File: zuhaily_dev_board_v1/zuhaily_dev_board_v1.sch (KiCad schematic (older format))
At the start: 42 parts

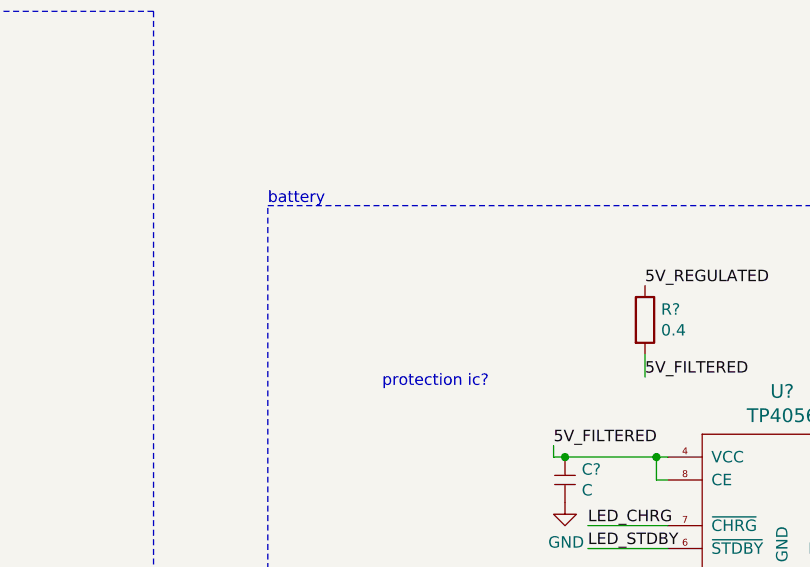
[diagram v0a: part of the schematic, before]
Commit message: added battery protection ic and testing git
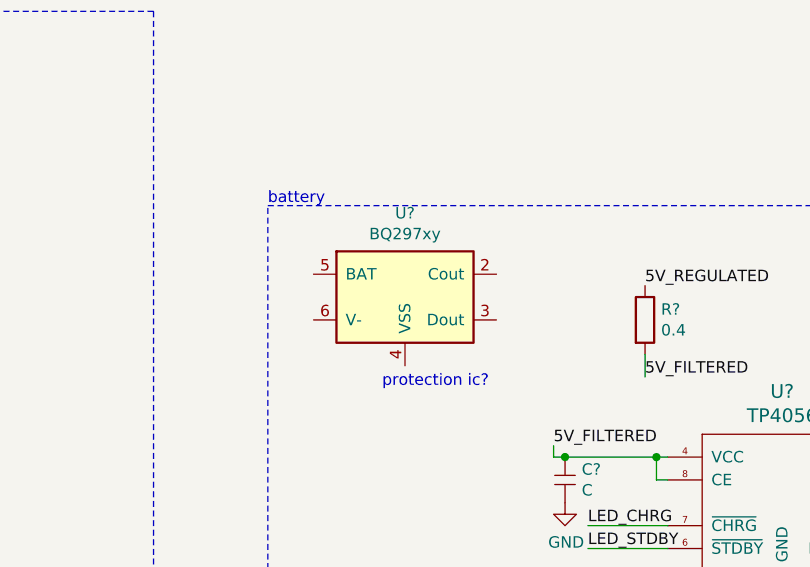
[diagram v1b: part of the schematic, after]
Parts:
- added U?: BQ297xy, Package_SON:WSON-6_1.5x1.5mm_P0.5mm, symbol Battery_Management:BQ297xy
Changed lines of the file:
@@
 Text Notes 17300 3150 0    50   ~ 0
 how to choose between usb vs batt?\n
+$Comp
+L Battery_Management:BQ297xy U?
+U 1 1 5C50F073
+P 15150 2550
+F 0 "U?" H 15150 2917 50  0000 C CNN
+F 1 "BQ297xy" H 15150 2826 50  0000 C CNN
+F 2 "Package_SON:WSON-6_1.5x1.5mm_P0.5mm" H 15150 2900 50  0001 C CNN
+F 3 "http://www.ti.com/lit/ds/symlink/bq2970.pdf" H 14900 2750 50  0001 C CNN
+	1    15150 2550
+	1    0    0    -1
+$EndComp
 $EndSCHEMATC

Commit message: added dc/usb switcher
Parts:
- added D?: DIODE, symbol pspice:DIODE
- added J?: DC_JACK, symbol tinkerforge:DC_JACK
- added Q?: MOSFET_P_CH, symbol tinkerforge:MOSFET_P_CH
- added R? (x2): 10K, symbol Device:R
- added U?: LMV358, symbol Amplifier_Operational:LMV358
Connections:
- net 3.3V_REGULATED: now also U?.2 (-)
- net 5V_REGULATED: now also Q?.D
- net GND: now also J?.1, J?.3, R?.2
- net USB_VCC: now also Q?.S; no longer U?.3 (VI)
- new net: D?.1 (K), J?.2
- new net: R?.1, R?.2, U?.3 (+)
- new net: Q?.G, U?.1
- new net 5V_REGULATOR_IN: D?.2 (A), R?.1, U?.3 (VI)
- no-connect marks 0 -> 1
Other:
- note added: "DC/usb switcher\n"
- note added: "also not sure why vin is divided by 2\n"
- note added: "not sure why it's compared to 3.3v\n"
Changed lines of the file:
@@
 EELAYER 26 0
 EELAYER END
-$Descr User 19685 11811
+$Descr User 39370 11811
 encoding utf-8
 Sheet 1 1
@@
 Wire Wire Line
 	4000 5700 3550 5700
-Text Label 3200 1650 0    50   ~ 0
-USB_VCC
-Wire Wire Line
-	3200 1650 3200 1850
+Text Label 3200 1550 0    50   ~ 0
+5V_REGULATOR_IN
+Wire Wire Line
+	3200 1550 3200 1850
 Text Label 4950 6100 0    50   ~ 0
 CH340_DTR
@@
 	1    0    0    -1
 $EndComp
+$Comp
+L tinkerforge:DC_JACK J?
+U 1 1 5C521394
+P 15250 6700
+F 0 "J?" H 15331 7037 60  0000 C CNN
+F 1 "DC_JACK" H 15331 6931 60  0000 C CNN
+F 2 "" H 15250 6700 60  0000 C CNN
+F 3 "" H 15250 6700 60  0000 C CNN
+	1    15250 6700
+	0    -1   -1   0
+$EndComp
+$Comp
+L power:GND #PWR?
+U 1 1 5C528256
+P 15200 6300
+F 0 "#PWR?" H 15200 6050 50  0001 C CNN
+F 1 "GND" H 15205 6127 50  0000 C CNN
+F 2 "" H 15200 6300 50  0001 C CNN
+F 3 "" H 15200 6300 50  0001 C CNN
+	1    15200 6300
+	0    -1   -1   0
+$EndComp
+Wire Wire Line
+	15200 6300 15200 6400
+Wire Wire Line
+	15200 6400 15450 6400
+Wire Wire Line
+	15450 6400 15450 6600
+Connection ~ 15200 6400
+NoConn ~ 17300 3550
+$Comp
+L pspice:DIODE D?
+U 1 1 5C5476D5
+P 15800 6750
+F 0 "D?" H 15800 7015 50  0000 C CNN
+F 1 "DIODE" H 15800 6924 50  0000 C CNN
+F 2 "" H 15800 6750 50  0001 C CNN
+F 3 "~" H 15800 6750 50  0001 C CNN
+	1    15800 6750
+	1    0    0    -1
+$EndComp
+Wire Wire Line
+	15600 6750 15450 6750
+$Comp
+L Device:R R?
+U 1 1 5C54DF04
+P 16650 6250
+F 0 "R?" H 16720 6296 50  0000 L CNN
+F 1 "10K" H 16720 6205 50  0000 L CNN
+F 2 "" V 16580 6250 50  0001 C CNN
+F 3 "~" H 16650 6250 50  0001 C CNN
+	1    16650 6250
+	1    0    0    -1
+$EndComp
+$Comp
+L Device:R R?
+U 1 1 5C54DF86
+P 16650 6700
+F 0 "R?" H 16720 6746 50  0000 L CNN
+F 1 "10K" H 16720 6655 50  0000 L CNN
+F 2 "" V 16580 6700 50  0001 C CNN
+F 3 "~" H 16650 6700 50  0001 C CNN
+	1    16650 6700
+	1    0    0    -1
+$EndComp
+Wire Wire Line
+	16650 6550 16650 6400
+Wire Wire Line
+	16000 6750 16000 6000
+Wire Wire Line
+	16000 6000 16650 6000
+Wire Wire Line
+	16650 6000 16650 6100
+$Comp
+L Amplifier_Operational:LMV358 U?
+U 1 1 5C5593EF
+P 17650 6650
+F 0 "U?" H 17650 7017 50  0000 C CNN
+F 1 "LMV358" H 17650 6926 50  0000 C CNN
+F 2 "" H 17650 6650 50  0001 C CNN
+F 3 "http://www.ti.com/lit/ds/symlink/lmv324.pdf" H 17650 6650 50  0001 C CNN
+	1    17650 6650
+	1    0    0    -1
+$EndComp
+Wire Wire Line
+	17350 6550 16650 6550
+Connection ~ 16650 6550
+$Comp
+L power:GND #PWR?
+U 1 1 5C55F888
+P 16650 6900
+F 0 "#PWR?" H 16650 6650 50  0001 C CNN
+F 1 "GND" H 16655 6727 50  0000 C CNN
+F 2 "" H 16650 6900 50  0001 C CNN
+F 3 "" H 16650 6900 50  0001 C CNN
+	1    16650 6900
+	1    0    0    -1
+$EndComp
+Wire Wire Line
+	16650 6900 16650 6850
+$Comp
+L tinkerforge:MOSFET_P_CH Q?
+U 1 1 5C56CE68
+P 18100 7500
+F 0 "Q?" V 18336 7500 50  0000 C CNN
+F 1 "MOSFET_P_CH" V 18427 7500 50  0000 C CNN
+F 2 "" H 18300 7600 50  0000 C CNN
+F 3 "" H 18100 7500 50  0000 C CNN
+	1    18100 7500
+	0    1    1    0
+$EndComp
+Text Label 17400 7600 0    50   ~ 0
+USB_VCC
+Wire Wire Line
+	17900 7600 17400 7600
+Wire Wire Line
+	17950 6650 18100 6650
+Wire Wire Line
+	18100 6650 18100 7300
+Text Label 16100 7500 0    50   ~ 0
+5V_REGULATOR_IN
+Wire Wire Line
+	16000 6750 16000 7500
+Wire Wire Line
+	16000 7500 16100 7500
+Connection ~ 16000 6750
+Text Label 18700 7500 0    50   ~ 0
+5V_REGULATED
+Wire Wire Line
+	18700 7500 18700 7600
+Wire Wire Line
+	18700 7600 18300 7600
+Wire Notes Line
+	19450 5850 19450 8050
+Wire Notes Line
+	19450 8050 14750 8050
+Wire Notes Line
+	14750 8050 14750 5850
+Wire Notes Line
+	14750 5850 19450 5850
+Text Notes 14800 5850 0    50   ~ 0
+DC/usb switcher\n
+Text Label 17150 7100 0    50   ~ 0
+3.3V_REGULATED
+Wire Wire Line
+	17150 7100 17150 6750
+Wire Wire Line
+	17150 6750 17350 6750
+Text Notes 16600 7250 0    50   ~ 0
+not  sure why it's compared to 3.3v\n
+Text Notes 16750 6100 0    50   ~ 0
+also not sure why vin is divided by 2\n
 $EndSCHEMATC

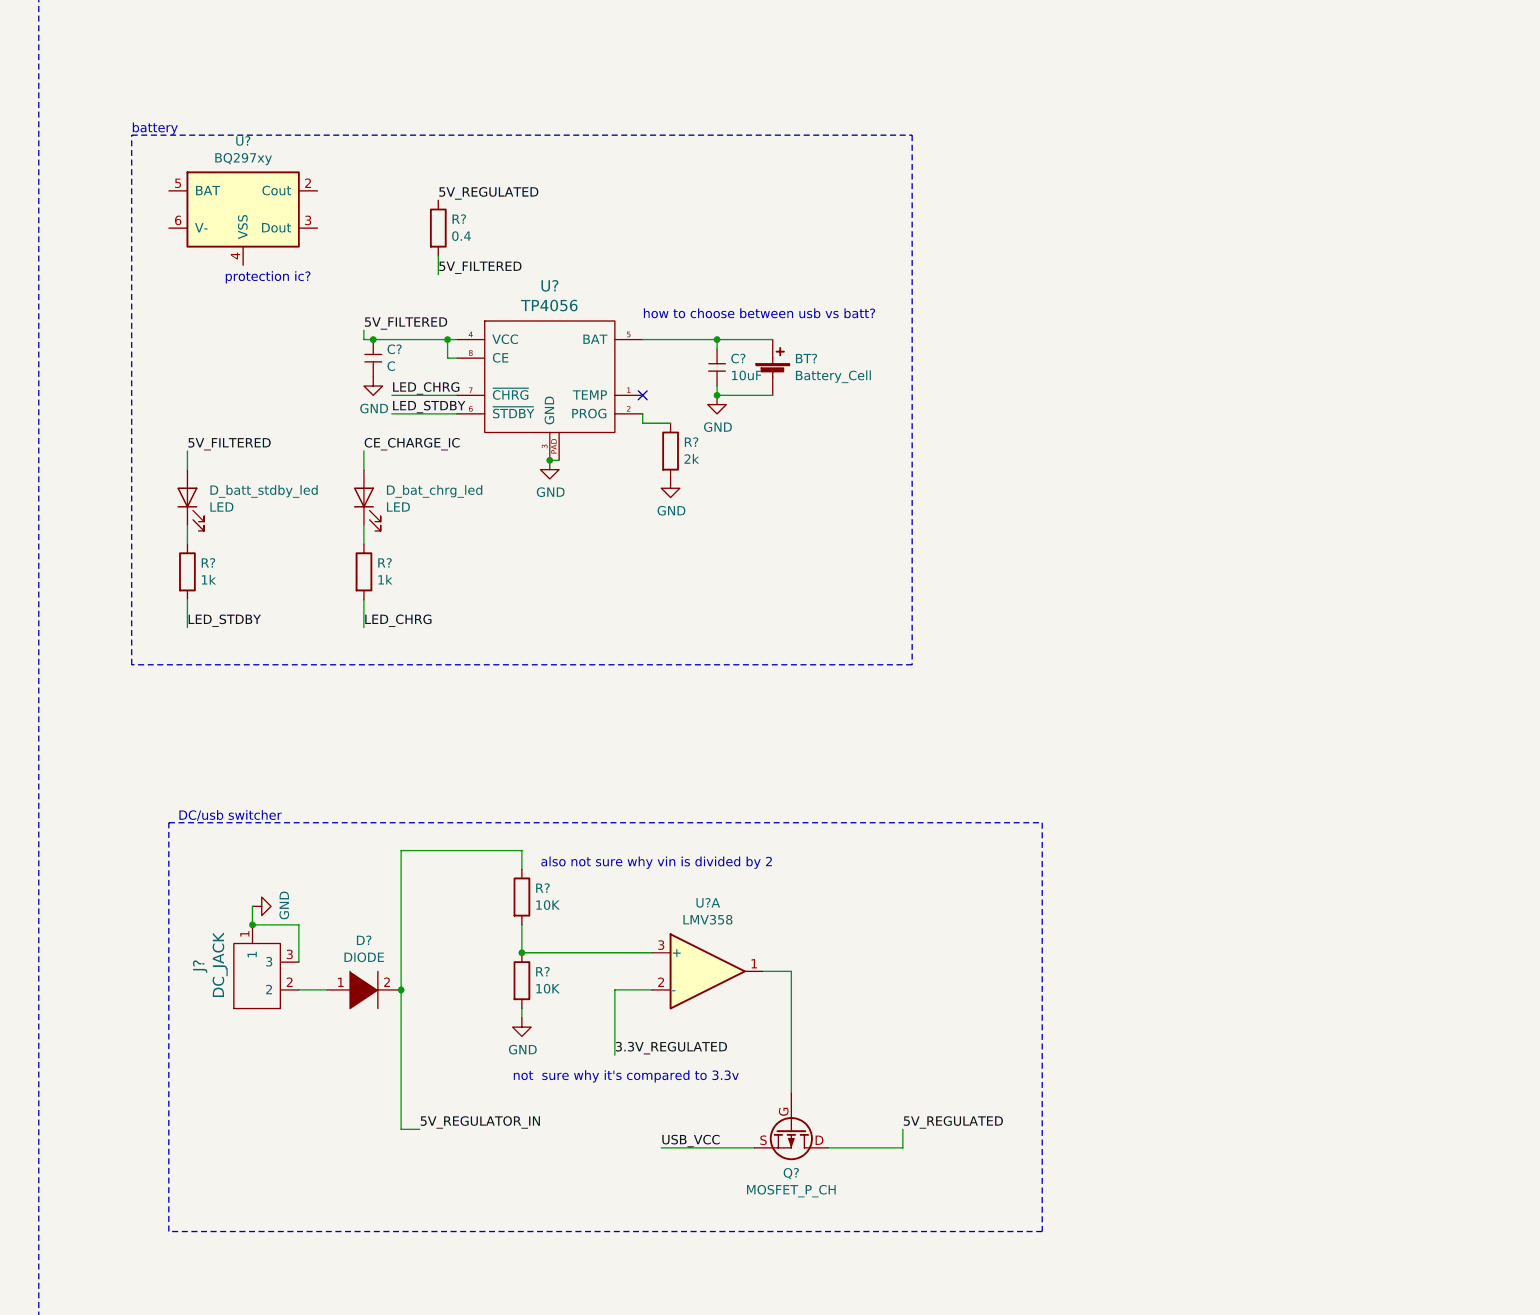
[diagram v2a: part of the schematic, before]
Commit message: added part of battery protection ic and some initial wiring
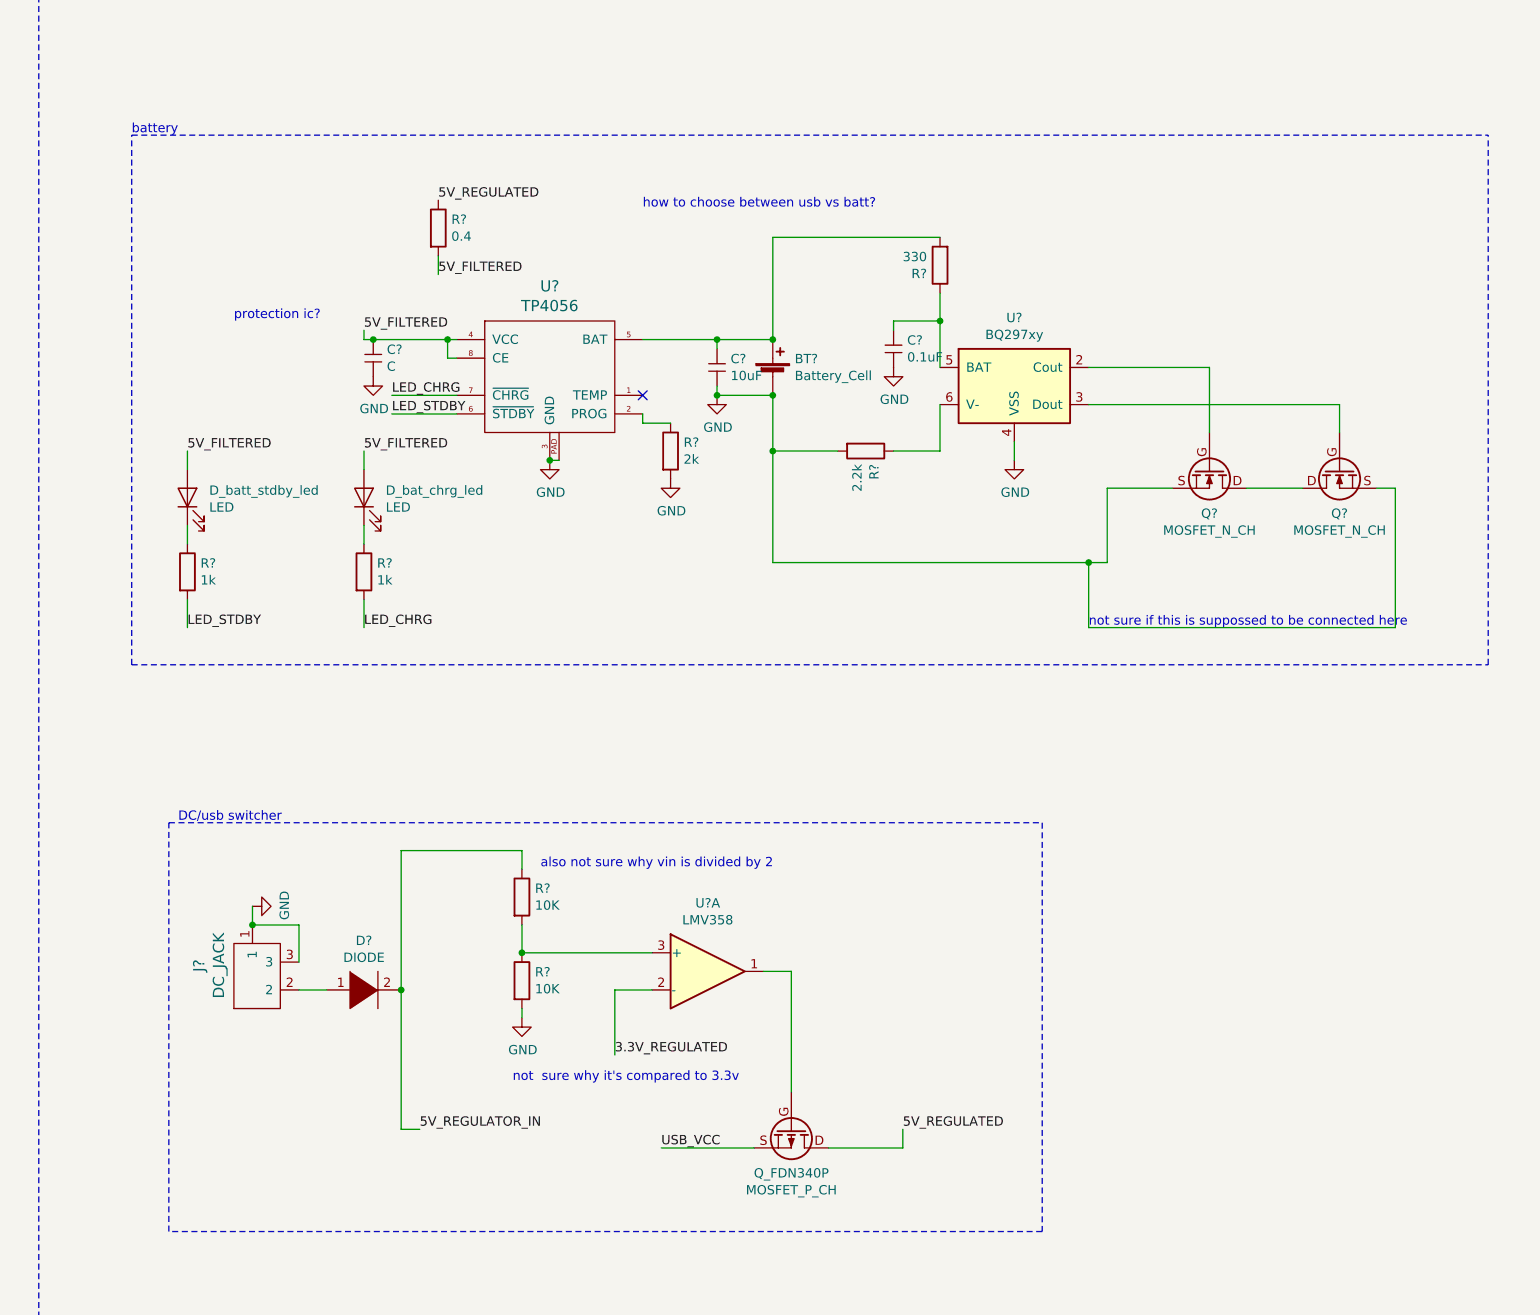
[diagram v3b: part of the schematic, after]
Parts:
- added C?: 0.1uF, symbol c:C
- added Q? (x2): MOSFET_N_CH, symbol tinkerforge:MOSFET_N_CH
- added R?: 2.2k, symbol Device:R
- added R?: 330, symbol Device:R
- gave numbers to parts that had none: 1
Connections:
- net CE_CHARGE_IC is gone; now on net 5V_FILTERED: D_bat_chrg_led.2 (A)
- net GND: now also U?.4 (VSS), C?.2, Q?.S, Q?.S, R?.2
- net at BT?.1 (+), C?.1, U?.5 (BAT): now also R?.2
- net at U?.2 (Cout): now also Q?.G
- net at U?.3 (Dout): now also Q?.G
- net at U?.5 (BAT): now also C?.1, R?.1
- net at U?.6 (V-): now also R?.1
- new net: Q?.D, Q?.D
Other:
- note added: "not sure if this is suppossed to be connected here\n"
- moved on the sheet: U?
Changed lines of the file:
@@
 $EndComp
-Wire Wire Line
-	15800 3200 15800 3250
 Wire Wire Line
 	15800 3250 15850 3250
@@
 	0    -1   -1   0
 $EndComp
-Text Label 15800 3850 0    50   ~ 0
-CE_CHARGE_IC
 Wire Wire Line
 	15800 3950 15800 3850
@@
 $EndComp
 Connection ~ 17700 3550
-Wire Notes Line
-	14550 2150 18750 2150
-Wire Notes Line
-	18750 2150 18750 5000
-Wire Notes Line
-	18750 5000 14550 5000
 Wire Notes Line
 	14550 5000 14550 2150
@@
 Text Notes 9700 9200 0    50   ~ 0
 esp 8266
-Text Notes 15050 2950 0    50   ~ 0
+Text Notes 15100 3150 0    50   ~ 0
 protection ic?\n
 Wire Wire Line
@@
 Wire Wire Line
 	10600 2850 10450 2850
-Text Notes 17300 3150 0    50   ~ 0
-how to choose between usb vs batt?\n
 $Comp
 L Battery_Management:BQ297xy U?
 U 1 1 5C50F073
-P 15150 2550
-F 0 "U?" H 15150 2917 50  0000 C CNN
-F 1 "BQ297xy" H 15150 2826 50  0000 C CNN
-F 2 "Package_SON:WSON-6_1.5x1.5mm_P0.5mm" H 15150 2900 50  0001 C CNN
-F 3 "http://www.ti.com/lit/ds/symlink/bq2970.pdf" H 14900 2750 50  0001 C CNN
-	1    15150 2550
+P 19300 3500
+F 0 "U?" H 19300 3867 50  0000 C CNN
+F 1 "BQ297xy" H 19300 3776 50  0000 C CNN
+F 2 "Package_SON:WSON-6_1.5x1.5mm_P0.5mm" H 19300 3850 50  0001 C CNN
+F 3 "http://www.ti.com/lit/ds/symlink/bq2970.pdf" H 19050 3700 50  0001 C CNN
+	1    19300 3500
 	1    0    0    -1
 $EndComp
@@
 	16650 6900 16650 6850
 $Comp
-L tinkerforge:MOSFET_P_CH Q?
+L tinkerforge:MOSFET_P_CH Q_FDN340P
 U 1 1 5C56CE68
 P 18100 7500
-F 0 "Q?" V 18336 7500 50  0000 C CNN
+F 0 "Q_FDN340P" V 18336 7500 50  0000 C CNN
 F 1 "MOSFET_P_CH" V 18427 7500 50  0000 C CNN
 F 2 "" H 18300 7600 50  0000 C CNN
@@
 Text Notes 16750 6100 0    50   ~ 0
 also not sure why vin is divided by 2\n
+Wire Wire Line
+	15800 3250 15800 3200
+Text Label 15800 3850 0    50   ~ 0
+5V_FILTERED
+$Comp
+L Device:R R?
+U 1 1 5C5EC1A2
+P 18500 3850
+F 0 "R?" H 18570 3896 50  0000 L CNN
+F 1 "2.2k" H 18570 3805 50  0000 L CNN
+F 2 "" V 18430 3850 50  0001 C CNN
+F 3 "~" H 18500 3850 50  0001 C CNN
+	1    18500 3850
+	0    1    1    0
+$EndComp
+Wire Wire Line
+	18900 3600 18900 3850
+Wire Wire Line
+	18900 3850 18650 3850
+Wire Wire Line
+	18350 3850 18000 3850
+Wire Wire Line
+	18000 3850 18000 3550
+Connection ~ 18000 3550
+$Comp
+L power:GND #PWR?
+U 1 1 5C5F9BA8
+P 19300 3900
+F 0 "#PWR?" H 19300 3650 50  0001 C CNN
+F 1 "GND" H 19305 3727 50  0000 C CNN
+F 2 "" H 19300 3900 50  0001 C CNN
+F 3 "" H 19300 3900 50  0001 C CNN
+	1    19300 3900
+	1    0    0    -1
+$EndComp
+Wire Wire Line
+	19300 3900 19300 3800
+$Comp
+L tinkerforge:MOSFET_N_CH Q?
+U 1 1 5C6017A2
+P 20350 3950
+F 0 "Q?" V 20586 3950 50  0000 C CNN
+F 1 "MOSFET_N_CH" V 20677 3950 50  0000 C CNN
+F 2 "" H 20550 4050 50  0000 C CNN
+F 3 "" H 20350 3950 50  0000 C CNN
+	1    20350 3950
+	0    1    1    0
+$EndComp
+$Comp
+L tinkerforge:MOSFET_N_CH Q?
+U 1 1 5C601C79
+P 21050 3950
+F 0 "Q?" V 21286 3950 50  0000 C CNN
+F 1 "MOSFET_N_CH" V 21377 3950 50  0000 C CNN
+F 2 "" H 21250 4050 50  0000 C CNN
+F 3 "" H 21050 3950 50  0000 C CNN
+	1    21050 3950
+	0    -1   1    0
+$EndComp
+Wire Wire Line
+	20850 4050 20550 4050
+Wire Wire Line
+	20350 3750 20350 3400
+Wire Wire Line
+	20350 3400 19700 3400
+Wire Wire Line
+	21050 3750 21050 3600
+Wire Wire Line
+	21050 3600 19700 3600
+Wire Wire Line
+	20150 4050 19800 4050
+Wire Wire Line
+	19800 4050 19800 4450
+$Comp
+L Device:R R?
+U 1 1 5C61EB36
+P 18900 2850
+F 0 "R?" H 18970 2896 50  0000 L CNN
+F 1 "330" H 18970 2805 50  0000 L CNN
+F 2 "" V 18830 2850 50  0001 C CNN
+F 3 "~" H 18900 2850 50  0001 C CNN
+	1    18900 2850
+	-1   0    0    1
+$EndComp
+Wire Wire Line
+	18900 3000 18900 3150
+Text Notes 17300 2550 0    50   ~ 0
+how to choose between usb vs batt?\n
+Wire Wire Line
+	18000 3250 18000 2700
+Wire Wire Line
+	18000 2700 18900 2700
+Connection ~ 18000 3250
+$Comp
+L c:C C?
+U 1 1 5C634B89
+P 18650 3200
+F 0 "C?" H 18723 3146 50  0000 L CNN
+F 1 "0.1uF" H 18723 3055 50  0000 L CNN
+F 2 "" H 18550 3350 60  0000 C CNN
+F 3 "" H 18550 3350 60  0000 C CNN
+	1    18650 3200
+	1    0    0    -1
+$EndComp
+Wire Wire Line
+	18900 3150 18650 3150
+Wire Wire Line
+	18650 3150 18650 3200
+Connection ~ 18900 3150
+Wire Wire Line
+	18900 3150 18900 3400
+$Comp
+L power:GND #PWR?
+U 1 1 5C63BF33
+P 18650 3400
+F 0 "#PWR?" H 18650 3150 50  0001 C CNN
+F 1 "GND" H 18655 3227 50  0000 C CNN
+F 2 "" H 18650 3400 50  0001 C CNN
+F 3 "" H 18650 3400 50  0001 C CNN
+	1    18650 3400
+	1    0    0    -1
+$EndComp
+Wire Wire Line
+	21350 4050 21250 4050
+Wire Wire Line
+	18000 4450 18000 3850
+Wire Wire Line
+	18000 4450 19700 4450
+Connection ~ 18000 3850
+Wire Wire Line
+	21350 4050 21350 4800
+Wire Wire Line
+	21350 4800 19700 4800
+Wire Wire Line
+	19700 4800 19700 4450
+Connection ~ 19700 4450
+Wire Wire Line
+	19700 4450 19800 4450
+Text Notes 19700 4800 0    50   ~ 0
+not sure if this is suppossed to be connected here\n
+Wire Notes Line
+	21850 5000 21850 2150
+Wire Notes Line
+	14550 2150 21850 2150
+Wire Notes Line
+	14550 5000 21850 5000
 $EndSCHEMATC
